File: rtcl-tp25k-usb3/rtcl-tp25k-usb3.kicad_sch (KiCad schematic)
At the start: 105 parts, among them J1 ZX360D-B-10P(30), J10 SSQ-106-02-F-D-RA, J2 CF20221V0R0-NH, J3 DF40C(2.0)-60DS-0.4V(51), J4 DF40C(2.0)-60DS-0.4V(51), J5 JTAG, J6 Conn_01x02, J7 Conn_01x03, Q2 NTK3134NT1G, Q3 NTK3134NT1G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

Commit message: WIP
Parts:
- RN1, RN2, RN3, RN4, RN5, RN6, RN7, RN8, RN9: footprint rtcl-tp25k-usb3:RES_YC104_YAG -> rtcl-tp25k-usb3:ARRAY_FR-072K2L_YAG
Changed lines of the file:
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@@
 			)
 		)
-		(property "Footprint" "rtcl-tp25k-usb3:RES_YC104_YAG"
+		(property "Footprint" "rtcl-tp25k-usb3:ARRAY_FR-072K2L_YAG"
 			(at 189.23 57.785 90)
 			(hide yes)
@@
 			)
 		)
-		(property "Footprint" "rtcl-tp25k-usb3:RES_YC104_YAG"
+		(property "Footprint" "rtcl-tp25k-usb3:ARRAY_FR-072K2L_YAG"
 			(at 189.23 160.655 90)
 			(hide yes)
@@
 			)
 		)
-		(property "Footprint" "rtcl-tp25k-usb3:RES_YC104_YAG"
+		(property "Footprint" "rtcl-tp25k-usb3:ARRAY_FR-072K2L_YAG"
 			(at 189.23 130.175 90)
 			(hide yes)
@@
 			)
 		)
-		(property "Footprint" "rtcl-tp25k-usb3:RES_YC104_YAG"
+		(property "Footprint" "rtcl-tp25k-usb3:ARRAY_FR-072K2L_YAG"
 			(at 189.23 196.215 90)
 			(hide yes)
@@
 			)
 		)
-		(property "Footprint" "rtcl-tp25k-usb3:RES_YC104_YAG"
+		(property "Footprint" "rtcl-tp25k-usb3:ARRAY_FR-072K2L_YAG"
 			(at 189.23 104.775 90)
 			(hide yes)
@@
 			)
 		)
-		(property "Footprint" "rtcl-tp25k-usb3:RES_YC104_YAG"
+		(property "Footprint" "rtcl-tp25k-usb3:ARRAY_FR-072K2L_YAG"
 			(at 189.23 140.335 90)
 			(hide yes)
@@
 			)
 		)
-		(property "Footprint" "rtcl-tp25k-usb3:RES_YC104_YAG"
+		(property "Footprint" "rtcl-tp25k-usb3:ARRAY_FR-072K2L_YAG"
 			(at 189.23 170.815 90)
 			(hide yes)
@@
 			)
 		)
-		(property "Footprint" "rtcl-tp25k-usb3:RES_YC104_YAG"
+		(property "Footprint" "rtcl-tp25k-usb3:ARRAY_FR-072K2L_YAG"
 			(at 189.23 186.055 90)
 			(hide yes)
@@
 			)
 		)
-		(property "Footprint" "rtcl-tp25k-usb3:RES_YC104_YAG"
+		(property "Footprint" "rtcl-tp25k-usb3:ARRAY_FR-072K2L_YAG"
 			(at 189.23 114.935 90)
 			(hide yes)

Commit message: WIP
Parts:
- Q2, Q3, Q4, Q5, Q6: footprint Package_TO_SOT_SMD:SOT-723 -> rtcl-tp25k-usb3:SOT-723
- X1: LCSC (none) -> C1986781
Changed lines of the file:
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@@
 			)
 		)
-		(property "Footprint" "Package_TO_SOT_SMD:SOT-723"
+		(property "Footprint" "rtcl-tp25k-usb3:SOT-723"
 			(at 96.012 231.14 90)
 			(hide yes)
@@
 			)
 		)
-		(property "Footprint" "Package_TO_SOT_SMD:SOT-723"
+		(property "Footprint" "rtcl-tp25k-usb3:SOT-723"
 			(at 46.482 265.43 90)
 			(hide yes)
@@
 			)
 		)
-		(property "Footprint" "Package_TO_SOT_SMD:SOT-723"
+		(property "Footprint" "rtcl-tp25k-usb3:SOT-723"
 			(at 244.602 132.08 90)
 			(hide yes)
@@
 			)
 		)
-		(property "Footprint" "Package_TO_SOT_SMD:SOT-723"
+		(property "Footprint" "rtcl-tp25k-usb3:SOT-723"
 			(at 96.012 265.43 90)
 			(hide yes)
@@
 			)
 		)
+		(property "LCSC" "C1986781"
+			(at 72.39 165.1 0)
+			(hide yes)
+			(show_name no)
+			(do_not_autoplace no)
+			(effects
+				(font
+					(size 1.27 1.27)
+				)
+			)
+		)
 		(pin "2"
 		)
@@
 			)
 		)
-		(property "Footprint" "Package_TO_SOT_SMD:SOT-723"
+		(property "Footprint" "rtcl-tp25k-usb3:SOT-723"
 			(at 46.482 231.14 90)
 			(hide yes)

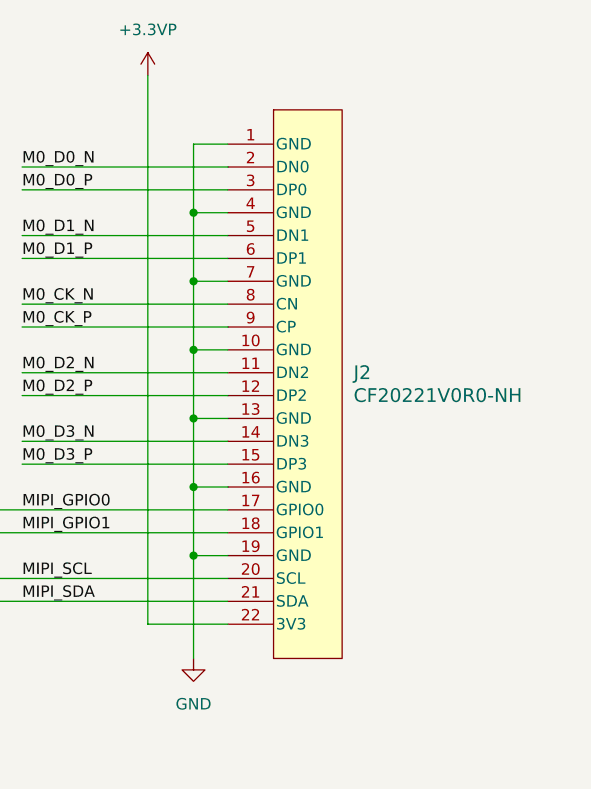
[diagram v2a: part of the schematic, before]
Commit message: Add RASPPICAM22_REV symbol and AFC11-S22ICA-00 footprint
- Introduced a new symbol "RASPPICAM22_REV" with properties including Reference, Value, Footprint, and LCSC.
- Added detailed pin definitions for the RASPPICAM22_REV symbol, including power, input, and output pins.
- Created a new footprint "AFC11-S22ICA-00" with defined pads and properties, including reference and value text.
- Included model path for the footprint to facilitate 3D visualization.
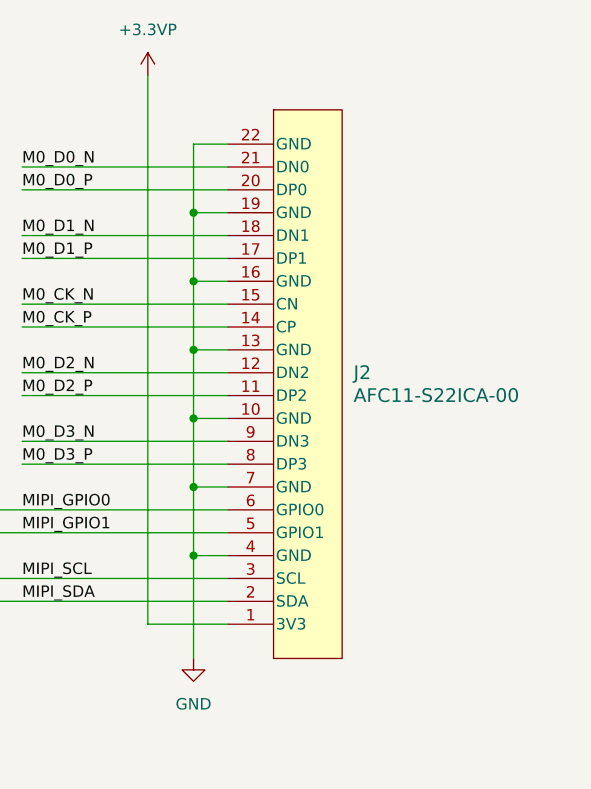
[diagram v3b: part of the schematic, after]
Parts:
- removed J2: CF20221V0R0-NH, rtcl-tp25k-usb3:CON_525592253_MOL, symbol rtcl-tp25k-usb3:RASPPICAM22
- added J2: AFC11-S22ICA-00, rtcl-tp25k-usb3:AFC11-S22ICA-00, symbol rtcl-tp25k-usb3:RASPPICAM22_REV
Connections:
- net +3.3VP: now also J2.1 (3V3)
- net A1_IOB24A_40P: now also J2.6 (GPIO0)
- net E3_IOB60A_40P: now also J2.5 (GPIO1)
- net GND: now also J2.10 (GND), J2.13 (GND), J2.16 (GND), J2.19 (GND), J2.22 (GND), J2.4 (GND), J2.7 (GND)
- net M0_CK_N: now also J2.15 (CN)
- net M0_CK_P: now also J2.14 (CP)
- net M0_D0_N: now also J2.21 (DN0)
- net M0_D0_P: now also J2.20 (DP0)
- net M0_D1_N: now also J2.18 (DN1)
- net M0_D1_P: now also J2.17 (DP1)
- net M0_D2_N: now also J2.12 (DN2)
- net M0_D2_P: now also J2.11 (DP2)
- net M0_D3_N: now also J2.9 (DN3)
- net M0_D3_P: now also J2.8 (DP3)
- net MIPI_SCL: now also J2.3 (SCL)
- net MIPI_SDA: now also J2.2 (SDA)
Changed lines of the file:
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@@
 	)
 	(symbol
-		(lib_id "rtcl-tp25k-usb3:RASPPICAM22")
-		(at 379.73 27.94 0)
-		(unit 1)
-		(body_style 1)
-		(exclude_from_sim no)
-		(in_bom yes)
-		(on_board yes)
-		(in_pos_files yes)
-		(dnp no)
-		(fields_autoplaced yes)
-		(property "Reference" "J2"
-			(at 386.08 54.6099 0)
-			(show_name no)
-			(do_not_autoplace no)
-			(effects
-				(font
-					(size 1.524 1.524)
-				)
-				(justify left)
-			)
-		)
-		(property "Value" "CF20221V0R0-NH"
-			(at 386.08 57.1499 0)
-			(show_name no)
-			(do_not_autoplace no)
-			(effects
-				(font
-					(size 1.524 1.524)
-				)
-				(justify left)
-			)
-		)
-		(property "Footprint" "rtcl-tp25k-usb3:CON_525592253_MOL"
-			(at 381.254 16.002 0)
-			(hide yes)
-			(show_name no)
-			(do_not_autoplace no)
-			(effects
-				(font
-					(size 1.27 1.27)
-					(italic yes)
-				)
-			)
-		)
-		(property "Datasheet" ""
-			(at 379.984 18.796 0)
-			(hide yes)
-			(show_name no)
-			(do_not_autoplace no)
-			(effects
-				(font
-					(size 1.27 1.27)
-					(italic yes)
-				)
-			)
-		)
-		(property "Description" ""
-			(at 388.62 29.21 0)
-			(hide yes)
-			(show_name no)
-			(do_not_autoplace no)
-			(effects
-				(font
-					(size 1.27 1.27)
-				)
-			)
-		)
-		(property "LCSC" "C3169524"
-			(at 379.73 27.94 0)
-			(hide yes)
-			(show_name no)
-			(do_not_autoplace no)
-			(effects
-				(font
-					(size 1.27 1.27)
-				)
-			)
-		)
-		(pin "19"
-		)
-		(pin "22"
-		)
-		(pin "11"
-		)
-		(pin "7"
-		)
-		(pin "13"
-		)
-		(pin "3"
-		)
-		(pin "4"
-		)
-		(pin "10"
-		)
-		(pin "12"
-		)
-		(pin "5"
-		)
-		(pin "1"
-		)
-		(pin "14"
-		)
-		(pin "8"
-		)
-		(pin "16"
-		)
-		(pin "2"
-		)
-		(pin "21"
-		)
-		(pin "9"
-		)
-		(pin "15"
-		)
-		(pin "6"
-		)
-		(pin "17"
-		)
-		(pin "18"
-		)
-		(pin "20"
-		)
-		(instances
-			(project "rtcl-tp25k-usb3"
-				(path "/3111823c-3b86-4a35-a2d4-382a0824eec6"
-					(reference "J2")
-					(unit 1)
-				)
-			)
-		)
-	)
-	(symbol
 		(lib_id "power:PWR_FLAG")
 		(at 85.09 144.78 0)
@@
 					(unit 1)
 				)
+			)
+		)
+	)
+	(symbol
+		(lib_id "rtcl-tp25k-usb3:RASPPICAM22_REV")
+		(at 379.73 27.94 0)
+		(unit 1)
+		(body_style 1)
+		(exclude_from_sim no)
+		(in_bom yes)
+		(on_board yes)
+		(in_pos_files yes)
+		(dnp no)
+		(fields_autoplaced yes)
+		(property "Reference" "J2"
+			(at 386.08 54.6099 0)
+			(show_name no)
+			(do_not_autoplace no)
+			(effects
+				(font
+					(size 1.524 1.524)
+				)
+				(justify left)
+			)
+		)
+		(property "Value" "AFC11-S22ICA-00"
+			(at 386.08 57.1499 0)
+			(show_name no)
+			(do_not_autoplace no)
+			(effects
+				(font
+					(size 1.524 1.524)
+				)
+				(justify left)
+			)
+		)
+		(property "Footprint" "rtcl-tp25k-usb3:AFC11-S22ICA-00"
+			(at 381.254 16.002 0)
+			(hide yes)
+			(show_name no)
+			(do_not_autoplace no)
+			(effects
+				(font
+					(size 1.27 1.27)
+					(italic yes)
+				)
+			)
+		)
+		(property "Datasheet" ""
+			(at 379.984 18.796 0)
+			(hide yes)
+			(show_name no)
+			(do_not_autoplace no)
+			(effects
+				(font
+					(size 1.27 1.27)
+					(italic yes)
+				)
+			)
+		)
+		(property "Description" ""
+			(at 388.62 29.21 0)
+			(hide yes)
+			(show_name no)
+			(do_not_autoplace no)
+			(effects
+				(font
+					(size 1.27 1.27)
+				)
+			)
+		)
+		(property "LCSC" "C5248019"
+			(at 379.73 27.94 0)
+			(hide yes)
+			(show_name no)
+			(do_not_autoplace no)
+			(effects
+				(font
+					(size 1.27 1.27)
+				)
+			)
+		)
+		(pin "21"
+		)
+		(pin "8"
+		)
+		(pin "2"
+		)
+		(pin "4"
+		)
+		(pin "5"
+		)
+		(pin "9"
+		)
+		(pin "3"
+		)
+		(pin "11"
+		)
+		(pin "10"
+		)
+		(pin "14"
+		)
+		(pin "17"
+		)
+		(pin "15"
+		)
+		(pin "6"
+		)
+		(pin "16"
+		)
+		(pin "18"
+		)
+		(pin "1"
+		)
+		(pin "12"
+		)
+		(pin "13"
+		)
+		(pin "7"
+		)
+		(pin "19"
+		)
+		(pin "20"
+		)
+		(pin "22"
+		)
+		(instances
+			(project "rtcl-tp25k-usb3"
+				(path "/3111823c-3b86-4a35-a2d4-382a0824eec6"
+					(reference "J2")
+					(unit 1)
+				)

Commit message: Update KiCad project files: change active layer and modify selection filter settings
- Changed active layer from 0 to 25 in the .kicad_prl file.
- Updated selection filter settings to disable visibility for dimensions, footprints, graphics, keepouts, pads, text, tracks, and vias, while keeping locked items and zones visible.
- Modified visible layers string in the .kicad_prl file.
- Added a new property "LCSC" with value "C6332199" for a component in the .kicad_sch file.
- Updated the "LCSC" property value from "C37208" to "C2897426" for another component in the .kicad_sch file.
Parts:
- J10: LCSC C37208 -> C2897426
- J5: LCSC (none) -> C6332199
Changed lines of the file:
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@@
 			)
 		)
+		(property "LCSC" "C6332199"
+			(at 251.46 264.16 0)
+			(hide yes)
+			(show_name no)
+			(do_not_autoplace no)
+			(effects
+				(font
+					(size 1.27 1.27)
+				)
+			)
+		)
 		(pin "5"
 		)
@@
 			)
 		)
-		(property "LCSC" "C37208"
+		(property "LCSC" "C2897426"
 			(at 250.19 33.02 0)
 			(hide yes)

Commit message: Update PCB and schematic files with new component properties and adjustments
- Added LCSC properties for components C4364316, C15402, and C40059 in the PCB and schematic files.
- Adjusted reference positions for capacitors C24 and C7, and resistors R60 and R61 for better alignment.
- Updated the value property for components from "AFC11-S22ICA-00" to "MIPI_22pin" and "SSQ-106-02-F-D-RA" to "PMOD".
- Modified selection filter settings in the PCB layout to enable graphics and text visibility while disabling locked items and zones.
- Adjusted graphical elements in the PCB layout for improved clarity and alignment.
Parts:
- C73: LCSC (none) -> C40059
- J10: value SSQ-106-02-F-D-RA -> PMOD
- J2: value AFC11-S22ICA-00 -> MIPI_22pin
- R52: LCSC (none) -> C15402
- SW3: LCSC (none) -> C4364316
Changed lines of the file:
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@@
 			)
 		)
+		(property "LCSC" "C15402"
+			(at 40.64 199.39 90)
+			(hide yes)
+			(show_name no)
+			(do_not_autoplace no)
+			(effects
+				(font
+					(size 1.27 1.27)
+				)
+			)
+		)
 		(pin "1"
 		)
@@
 			)
 		)
+		(property "LCSC" "C40059"
+			(at 334.01 120.65 0)
+			(hide yes)
+			(show_name no)
+			(do_not_autoplace no)
+			(effects
+				(font
+					(size 1.27 1.27)
+				)
+			)
+		)
 		(pin "1"
 		)
@@
 			)
 		)
-		(property "Value" "AFC11-S22ICA-00"
+		(property "Value" "MIPI_22pin"
 			(at 386.08 57.1499 0)
 			(show_name no)
@@
 			)
 		)
+		(property "LCSC" "C4364316"
+			(at 195.58 260.35 0)
+			(hide yes)
+			(show_name no)
+			(do_not_autoplace no)
+			(effects
+				(font
+					(size 1.27 1.27)
+				)
+			)
+		)
 		(pin "1"
 		)
@@
 			)
 		)
-		(property "Value" "SSQ-106-02-F-D-RA"
+		(property "Value" "PMOD"
 			(at 251.46 24.13 0)
 			(show_name no)

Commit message: 発注時にWebで直した部分など修正
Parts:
- SW3: LCSC C4364316 -> C2961921
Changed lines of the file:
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@@
 			)
 		)
-		(property "LCSC" "C4364316"
+		(property "LCSC" "C2961921"
 			(at 195.58 260.35 0)
 			(hide yes)

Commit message: YC124-FR-0722RL に変更
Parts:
- RN1, RN2, RN3, RN4, RN5, RN6, RN7, RN8, RN9: value YC104-JR-0722RL -> YC124-FR-0722RL; footprint rtcl-tp25k-usb3:ARRAY_FR-072K2L_YAG -> rtcl-tp25k-usb3:RES_YC124_2X1_YAG
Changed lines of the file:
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@@
 			)
 		)
-		(property "Value" "YC104-JR-0722RL"
+		(property "Value" "YC124-FR-0722RL"
 			(at 189.23 57.15 90)
 			(show_name no)
@@
 			)
 		)
-		(property "Footprint" "rtcl-tp25k-usb3:ARRAY_FR-072K2L_YAG"
+		(property "Footprint" "rtcl-tp25k-usb3:RES_YC124_2X1_YAG"
 			(at 189.23 57.785 90)
 			(hide yes)
@@
 			)
 		)
-		(property "Value" "YC104-JR-0722RL"
+		(property "Value" "YC124-FR-0722RL"
 			(at 175.768 161.544 90)
 			(show_name no)
@@
 			)
 		)
-		(property "Footprint" "rtcl-tp25k-usb3:ARRAY_FR-072K2L_YAG"
+		(property "Footprint" "rtcl-tp25k-usb3:RES_YC124_2X1_YAG"
 			(at 189.23 160.655 90)
 			(hide yes)
@@
 			)
 		)
-		(property "Value" "YC104-JR-0722RL"
+		(property "Value" "YC124-FR-0722RL"
 			(at 176.53 131.064 90)
 			(show_name no)
@@
 			)
 		)
-		(property "Footprint" "rtcl-tp25k-usb3:ARRAY_FR-072K2L_YAG"
+		(property "Footprint" "rtcl-tp25k-usb3:RES_YC124_2X1_YAG"
 			(at 189.23 130.175 90)
 			(hide yes)
@@
 			)
 		)
-		(property "Value" "YC104-JR-0722RL"
+		(property "Value" "YC124-FR-0722RL"
 			(at 175.514 211.328 90)
 			(show_name no)
@@
 			)
 		)
-		(property "Footprint" "rtcl-tp25k-usb3:ARRAY_FR-072K2L_YAG"
+		(property "Footprint" "rtcl-tp25k-usb3:RES_YC124_2X1_YAG"
 			(at 189.23 196.215 90)
 			(hide yes)
@@
 			)
 		)
-		(property "Value" "YC104-JR-0722RL"
+		(property "Value" "YC124-FR-0722RL"
 			(at 176.53 105.918 90)
 			(show_name no)
@@
 			)
 		)
-		(property "Footprint" "rtcl-tp25k-usb3:ARRAY_FR-072K2L_YAG"
+		(property "Footprint" "rtcl-tp25k-usb3:RES_YC124_2X1_YAG"
 			(at 189.23 104.775 90)
 			(hide yes)
@@
 			)
 		)
-		(property "Value" "YC104-JR-0722RL"
+		(property "Value" "YC124-FR-0722RL"
 			(at 175.768 154.178 90)
 			(show_name no)
@@
 			)
 		)
-		(property "Footprint" "rtcl-tp25k-usb3:ARRAY_FR-072K2L_YAG"
+		(property "Footprint" "rtcl-tp25k-usb3:RES_YC124_2X1_YAG"
 			(at 189.23 140.335 90)
 			(hide yes)
@@
 			)
 		)
-		(property "Value" "YC104-JR-0722RL"
+		(property "Value" "YC124-FR-0722RL"
 			(at 176.53 184.912 90)
 			(show_name no)
@@
 			)
 		)
-		(property "Footprint" "rtcl-tp25k-usb3:ARRAY_FR-072K2L_YAG"
+		(property "Footprint" "rtcl-tp25k-usb3:RES_YC124_2X1_YAG"
 			(at 189.23 170.815 90)
 			(hide yes)
@@
 			)
 		)
-		(property "Value" "YC104-JR-0722RL"
+		(property "Value" "YC124-FR-0722RL"
 			(at 176.53 186.944 90)
 			(show_name no)
@@
 			)
 		)
-		(property "Footprint" "rtcl-tp25k-usb3:ARRAY_FR-072K2L_YAG"
+		(property "Footprint" "rtcl-tp25k-usb3:RES_YC124_2X1_YAG"
 			(at 189.23 186.055 90)
 			(hide yes)
@@
 			)
 		)
-		(property "Value" "YC104-JR-0722RL"
+		(property "Value" "YC124-FR-0722RL"
 			(at 176.53 128.778 90)
 			(show_name no)
@@
 			)
 		)
-		(property "Footprint" "rtcl-tp25k-usb3:ARRAY_FR-072K2L_YAG"
+		(property "Footprint" "rtcl-tp25k-usb3:RES_YC124_2X1_YAG"
 			(at 189.23 114.935 90)
 			(hide yes)

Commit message: update
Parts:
- Q2, Q3, Q4, Q5, Q6: footprint rtcl-tp25k-usb3:SOT-723 -> rtcl-tp25k-usb3:SOT_34NT1G_ONS
- RN1, RN2, RN3, RN5, RN6, RN7, RN8, RN9: LCSC (none) -> C309675
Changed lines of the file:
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@@
 			)
 		)
+		(property "LCSC" "C309675"
+			(at 189.23 64.77 90)
+			(hide yes)
+			(show_name no)
+			(do_not_autoplace no)
+			(effects
+				(font
+					(size 1.27 1.27)
+				)
+			)
+		)
 		(pin "3"
 		)
@@
 			)
 		)
+		(property "LCSC" "C309675"
+			(at 189.23 167.64 90)
+			(hide yes)
+			(show_name no)
+			(do_not_autoplace no)
+			(effects
+				(font
+					(size 1.27 1.27)
+				)
+			)
+		)
 		(pin "3"
 		)
@@
 			)
 		)
-		(property "Footprint" "rtcl-tp25k-usb3:SOT-723"
+		(property "Footprint" "rtcl-tp25k-usb3:SOT_34NT1G_ONS"
 			(at 96.012 231.14 90)
 			(hide yes)
@@
 			)
 		)
-		(property "Footprint" "rtcl-tp25k-usb3:SOT-723"
+		(property "Footprint" "rtcl-tp25k-usb3:SOT_34NT1G_ONS"
 			(at 46.482 265.43 90)
 			(hide yes)
@@
 			)
 		)
-		(property "Footprint" "rtcl-tp25k-usb3:SOT-723"
+		(property "Footprint" "rtcl-tp25k-usb3:SOT_34NT1G_ONS"
 			(at 244.602 132.08 90)
 			(hide yes)
@@
 			)
 		)
-		(property "Footprint" "rtcl-tp25k-usb3:SOT-723"
+		(property "Footprint" "rtcl-tp25k-usb3:SOT_34NT1G_ONS"
 			(at 96.012 265.43 90)
 			(hide yes)
@@
 			)
 		)
+		(property "LCSC" "C309675"
+			(at 189.23 203.2 90)
+			(hide yes)
+			(show_name no)
+			(do_not_autoplace no)
+			(effects
+				(font
+					(size 1.27 1.27)
+				)
+			)
+		)
 		(pin "3"
 		)
@@
 			)
 		)
+		(property "LCSC" "C309675"
+			(at 189.23 111.76 90)
+			(hide yes)
+			(show_name no)
+			(do_not_autoplace no)
+			(effects
+				(font
+					(size 1.27 1.27)
+				)
+			)
+		)
 		(pin "3"
 		)
@@
 			)
 		)
+		(property "LCSC" "C309675"
+			(at 189.23 147.32 90)
+			(hide yes)
+			(show_name no)
+			(do_not_autoplace no)
+			(effects
+				(font
+					(size 1.27 1.27)
+				)
+			)
+		)
 		(pin "3"
 		)
@@
 			)
 		)
+		(property "LCSC" "C309675"
+			(at 189.23 177.8 90)
+			(hide yes)
+			(show_name no)
+			(do_not_autoplace no)
+			(effects
+				(font
+					(size 1.27 1.27)
+				)
+			)
+		)
 		(pin "3"
 		)
@@
 			)
 		)
+		(property "LCSC" "C309675"
+			(at 189.23 193.04 90)
+			(hide yes)
+			(show_name no)
+			(do_not_autoplace no)
+			(effects
+				(font
+					(size 1.27 1.27)
+				)
+			)
+		)
 		(pin "3"
 		)
@@
 			)
 		)
-		(property "Footprint" "rtcl-tp25k-usb3:SOT-723"
+		(property "Footprint" "rtcl-tp25k-usb3:SOT_34NT1G_ONS"
 			(at 46.482 231.14 90)
 			(hide yes)
@@
 			(hide yes)
 			(show_name no)
+			(do_not_autoplace no)
+			(effects
+				(font
+					(size 1.27 1.27)
+				)
+			)
+		)
+		(property "LCSC" "C309675"
+			(at 189.23 121.92 90)
+			(hide yes)
+			(show_name no)
